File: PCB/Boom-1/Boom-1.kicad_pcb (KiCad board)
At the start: 2 copper layers, 698 parts, among them J1 NoiseIOConn, J10 Osc1HFTrackConn, J11 Osc1FiltCVConn, J12 OscFiltEnv1Conn, J13 OscFiltEnv2Conn, J14 SubFiltEnv1Conn, J15 SubFiltEnv2Conn, J16 Osc1FXConn, J17 SubFXConn, J18 Osc1FiltCVConn, J19 Osc1FiltCVConn, J2 Osc2CVConn, J20 Osc2FXConn, J21 OscAmpEnvConn, J22 SubAmpEnvConn, J23 OscAmpEnvBypass, J24 SubAmpAudioBypass, J25 SubAmpEnvBypass, J26 PreFV1FXConn, J27 PowerConn, J28 FV1Conn, J29 IOConn, J3 Osc1CVConn, J4 Osc2SyncConn, J5 Osc1SyncConn, J6 Osc2ScaleConn, J7 Osc2HFTrackConn, J8 SubIOConn, J9 Osc1ScaleConn, Q1 2N3904, SW1 SW_DIP_x04, U1 CEM3340, U10 AS3320, U11 AS3310, U12 AS3310, U13 AS3310, U14 AS3310, U15 V2164D, U16 AS3310, U17 AS3310, U18 V2164D, U19 TL074, U2 CEM3340, U20 TL074, U21 TL074, U22 TL074, U23 TL074, U24 TL074, U25 TL074, U26 TL074, U27 TL072, U28 TL074, U29 TL072, U3 4013, U30 TL074, U31 TL072, U32 TL074, U33 TL074, U34 TL074, U35 TL072, U36 TL074, U37 TL074, U38 TL072, U39 TL074, U4 NOISE, U40 TL072, U41 TL074, U42 TL074, U43 TL074, U44 TL074, U45 L7905, U46 L7805, U5 V2164D, U6 V2164D, U7 V2164D, U8 AS3320, U9 AS3320

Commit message: gathered componets for osc filt env 1
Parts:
- moved C86 1592.8 mm to (-516.1, -276.1)
- moved C55 1568.3 mm to (-506.5, -297.4)
- moved C61 1563.3 mm to (-515.9, -280.4)
- moved C85 1559.6 mm to (-496.1, -278.1)
- moved C69 1541.4 mm to (-483.9, -280.9)
- moved R173 1541.4 mm to (-486.2, -294.9)
- moved C57 1536.9 mm to (-516.1, -271.0)
- moved C70 1530.4 mm to (-465.8, -280.9)
- moved R182 1529.3 mm to (-487.4, -262.9)
- moved R176 1528.5 mm to (-486.2, -288.5)
- moved C78 1526.4 mm to (-442.7, -273.1), turned to 180 degrees
- moved R208 1518.1 mm to (-465.8, -273.1)
- moved C77 1512.7 mm to (-424.9, -280.7), turned to 180 degrees
- moved R148 1509.6 mm to (-511.0, -288.0), turned to 180 degrees
- moved R206 1508.2 mm to (-494.0, -285.5)
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
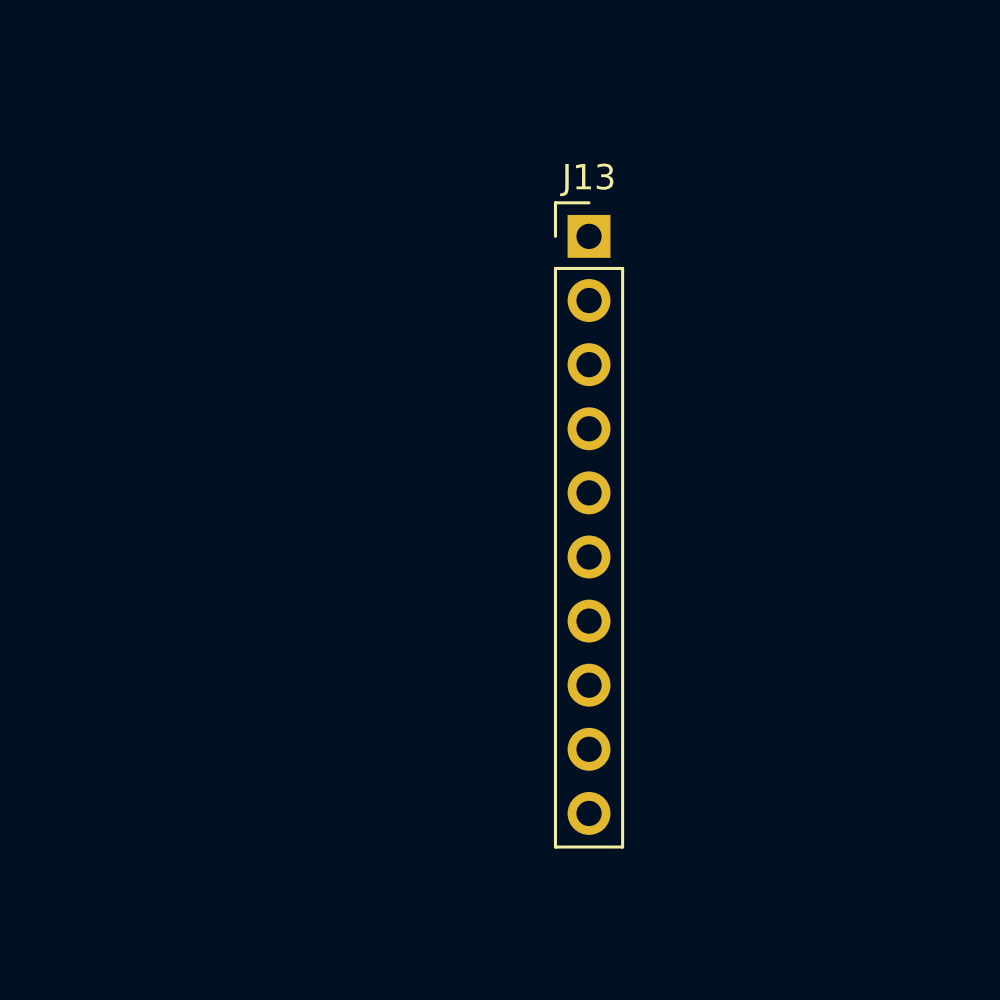
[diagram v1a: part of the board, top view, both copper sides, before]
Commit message: gathered componets for osc filt env 1
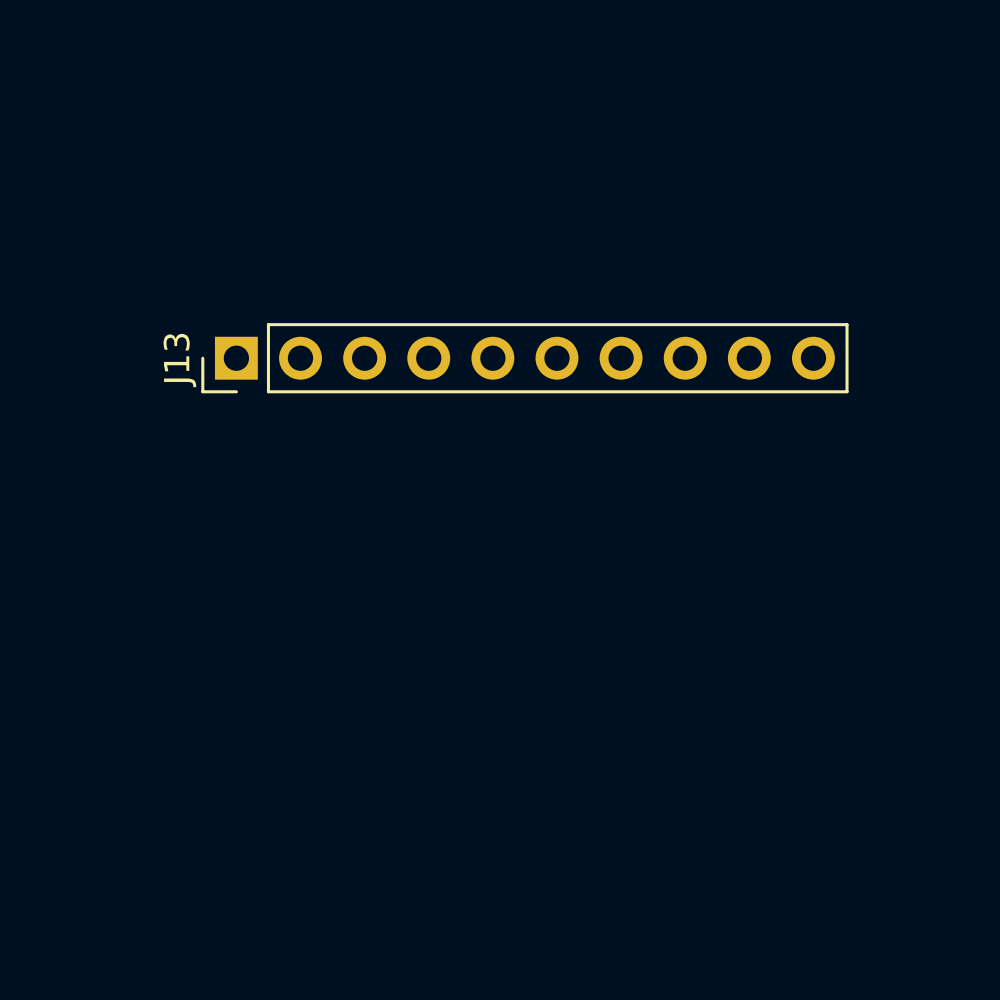
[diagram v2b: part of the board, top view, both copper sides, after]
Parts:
- moved J13 14.8 mm to (-478.3, -178.3), turned to 90 degrees
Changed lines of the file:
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@@
   )
   (module Connector_PinHeader_2.54mm:PinHeader_1x10_P2.54mm_Vertical (layer F.Cu)
-    (at -464.312 -183.134)
+    (at -478.282 -178.308 90)
     (descr "Through hole straight pin header, 1x10, 2.54mm pitch, single row")
     (tags "Through hole pin header THT 1x10 2.54mm single row")
-    (fp_text reference J13 (at 0 -2.33) (layer F.SilkS)
+    (fp_text reference J13 (at 0 -2.33 90) (layer F.SilkS)
       (effects (font (size 1 1) (thickness 0.15)))
     )
-    (fp_text value OscFiltEnv2Conn (at 0 25.19) (layer F.Fab)
+    (fp_text value OscFiltEnv2Conn (at 0 25.19 90) (layer F.Fab)
       (effects (font (size 1 1) (thickness 0.15)))
     )
@@
     (fp_line (start 1.8 24.65) (end 1.8 -1.8) (layer F.CrtYd) (width 0.05))
     (fp_line (start 1.8 -1.8) (end -1.8 -1.8) (layer F.CrtYd) (width 0.05))
-    (fp_text user %R (at 0 11.43 90) (layer F.Fab)
+    (fp_text user %R (at 0 11.43) (layer F.Fab)
       (effects (font (size 1 1) (thickness 0.15)))
     )
-    (pad 10 thru_hole oval (at 0 22.86) (size 1.7 1.7) (drill 1) (layers *.Cu *.Mask)
+    (pad 10 thru_hole oval (at 0 22.86 90) (size 1.7 1.7) (drill 1) (layers *.Cu *.Mask)
       (net 160 "Net-(J13-Pad10)"))
-    (pad 9 thru_hole oval (at 0 20.32) (size 1.7 1.7) (drill 1) (layers *.Cu *.Mask)
+    (pad 9 thru_hole oval (at 0 20.32 90) (size 1.7 1.7) (drill 1) (layers *.Cu *.Mask)
       (net 161 "Net-(J13-Pad9)"))
-    (pad 8 thru_hole oval (at 0 17.78) (size 1.7 1.7) (drill 1) (layers *.Cu *.Mask)
+    (pad 8 thru_hole oval (at 0 17.78 90) (size 1.7 1.7) (drill 1) (layers *.Cu *.Mask)
       (net 162 "Net-(J13-Pad8)"))
-    (pad 7 thru_hole oval (at 0 15.24) (size 1.7 1.7) (drill 1) (layers *.Cu *.Mask)
+    (pad 7 thru_hole oval (at 0 15.24 90) (size 1.7 1.7) (drill 1) (layers *.Cu *.Mask)
       (net 163 "Net-(J13-Pad7)"))
-    (pad 6 thru_hole oval (at 0 12.7) (size 1.7 1.7) (drill 1) (layers *.Cu *.Mask)
+    (pad 6 thru_hole oval (at 0 12.7 90) (size 1.7 1.7) (drill 1) (layers *.Cu *.Mask)
       (net 164 "Net-(J13-Pad6)"))
-    (pad 5 thru_hole oval (at 0 10.16) (size 1.7 1.7) (drill 1) (layers *.Cu *.Mask)
+    (pad 5 thru_hole oval (at 0 10.16 90) (size 1.7 1.7) (drill 1) (layers *.Cu *.Mask)
       (net 165 "Net-(J13-Pad5)"))
-    (pad 4 thru_hole oval (at 0 7.62) (size 1.7 1.7) (drill 1) (layers *.Cu *.Mask)
+    (pad 4 thru_hole oval (at 0 7.62 90) (size 1.7 1.7) (drill 1) (layers *.Cu *.Mask)
       (net 166 "Net-(J13-Pad4)"))
-    (pad 3 thru_hole oval (at 0 5.08) (size 1.7 1.7) (drill 1) (layers *.Cu *.Mask)
+    (pad 3 thru_hole oval (at 0 5.08 90) (size 1.7 1.7) (drill 1) (layers *.Cu *.Mask)
       (net 167 "Net-(J13-Pad3)"))
-    (pad 2 thru_hole oval (at 0 2.54) (size 1.7 1.7) (drill 1) (layers *.Cu *.Mask)
+    (pad 2 thru_hole oval (at 0 2.54 90) (size 1.7 1.7) (drill 1) (layers *.Cu *.Mask)
       (net 168 "Net-(J13-Pad2)"))
-    (pad 1 thru_hole rect (at 0 0) (size 1.7 1.7) (drill 1) (layers *.Cu *.Mask)
+    (pad 1 thru_hole rect (at 0 0 90) (size 1.7 1.7) (drill 1) (layers *.Cu *.Mask)
       (net 1 GND))
     (model ${KISYS3DMOD}/Connector_PinHeader_2.54mm.3dshapes/PinHeader_1x10_P2.54mm_Vertical.wrl

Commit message: gathered componets for osc filt env 2
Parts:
- moved C82 1555.2 mm to (-500.1, -232.2), turned to 180 degrees
- moved C56 1542.6 mm to (-515.4, -225.6)
- moved C81 1533.6 mm to (-505.7, -201.4)
- moved C58 1528.0 mm to (-515.6, -207.8)
- moved C62 1503.3 mm to (-515.1, -215.4)
- moved C68 1496.9 mm to (-474.5, -196.3)
- moved R152 1492.3 mm to (-496.3, -210.3)
- moved R207 1484.4 mm to (-467.4, -230.9), turned to 180 degrees
- moved R195 1484.0 mm to (-458.2, -224.5), turned to 180 degrees
- moved R174 1477.2 mm to (-486.9, -230.9)
- moved R185 1476.9 mm to (-458.2, -227.8)
- moved R228 1476.4 mm to (-455.4, -210.3)
- moved R149 1473.9 mm to (-516.4, -218.2), turned to 180 degrees
- moved C67 1471.1 mm to (-474.5, -202.7)
- moved R231 1469.9 mm to (-461.3, -216.9)
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
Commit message: gathered parts for sub filt env 1 and 2
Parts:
- moved C65 1323.3 mm to (-492.3, 236.7)
- moved C74 1299.9 mm to (-507.0, 350.3)
- moved R159 1287.0 mm to (-503.2, 249.2), turned to 180 degrees
- moved C66 1284.3 mm to (-501.9, 339.9), turned to 180 degrees
- moved C72 1274.6 mm to (-507.0, 357.6)
- moved R233 1268.0 mm to (-460.5, 242.3)
- moved C71 1261.3 mm to (-500.4, 259.3)
- moved R196 1260.0 mm to (-460.5, 238.0)
- moved R211 1242.9 mm to (-430.3, 238.0)
- moved C73 1236.4 mm to (-495.3, 251.7), turned to 180 degrees
- moved R199 1219.5 mm to (-463.0, 355.9)
- moved R210 1218.8 mm to (-430.0, 253.2)
- moved R212 1212.8 mm to (-430.3, 358.4)
- moved R221 1210.8 mm to (-432.6, 238.0), turned to 180 degrees
- moved R165 1206.7 mm to (-488.7, 355.1)
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
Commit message: gathered parts for osc amp env
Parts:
- moved C118 1109.2 mm to (-55.6, -82.8), turned to 180 degrees
- moved C120 1097.3 mm to (-60.7, -65.0)
- moved C115 1093.5 mm to (-60.7, -69.1)
- moved C122 1091.2 mm to (-55.6, -72.1), turned to 180 degrees
- moved C114 1089.1 mm to (-37.3, -70.6), turned to 180 degrees
- moved C143 1059.8 mm to (-8.64, -70.1), turned to 180 degrees
- moved C142 1055.9 mm to (8.64, -77.7), turned to 180 degrees
- moved C126 1028.1 mm to (45.0, -69.3)
- moved R267 1019.5 mm to (-55.6, -75.2), turned to 180 degrees
- moved C127 1014.3 mm to (62.5, -69.3)
- moved R269 998.6 mm to (-42.4, -67.6)
- moved R302 978.1 mm to (32.5, -65.0)
- moved R289 974.9 mm to (40.1, -62.0), turned to 180 degrees
- moved R308 962.8 mm to (42.4, -65.0)
- moved R290 958.9 mm to (79.5, -74.2), turned to 180 degrees
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
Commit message: power units for amp and filt envs
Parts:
- moved C88 1263.5 mm to (-452.9, 245.6), turned to 180 degrees
- moved C89 1224.0 mm to (-440.4, 245.6)
- moved C100 1180.6 mm to (-457.2, 296.4)
- moved C132 991.5 mm to (7.11, 20.6)
- moved C130 979.2 mm to (-11.9, 32.3)
- moved C133 964.5 mm to (24.6, 20.6)
- moved C135 961.8 mm to (5.59, 66.3)
- moved C137 955.7 mm to (-9.65, 53.8), turned to 180 degrees
- moved C134 950.8 mm to (27.9, 58.7), turned to 180 degrees
- moved C116 937.5 mm to (-17.5, 144.5)
- moved C117 923.9 mm to (-30.7, 144.5), turned to 180 degrees
- moved R277 919.7 mm to (-22.4, 25.4)
- moved C124 913.9 mm to (11.9, 140.5)
- moved C125 899.6 mm to (29.2, 140.5)
- moved C140 896.8 mm to (8.64, 173.7)
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
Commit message: gathered parts for osc amp
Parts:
- moved TP34 1046.6 mm to (-44.7, 31.0)
- moved C139 999.5 mm to (11.9, 25.9), turned to 270 degrees
- moved C128 996.6 mm to (-33.0, 30.5), turned to 180 degrees
- moved TP37 991.4 mm to (14.7, 35.6)
- moved C129 987.5 mm to (-31.8, 62.0), turned to 90 degrees
- moved R279 941.4 mm to (-37.3, 24.4)
- moved R278 917.4 mm to (-32.8, 39.9)
- moved R271 910.5 mm to (-25.1, 34.8), turned to 180 degrees
- moved R287 909.8 mm to (-35.6, 37.1), turned to 180 degrees
- moved R301 908.2 mm to (7.11, 25.7), turned to 270 degrees
- moved R272 905.2 mm to (-32.8, 47.5)
- moved R274 904.1 mm to (-25.1, 55.6), turned to 270 degrees
- moved R310 897.1 mm to (12.4, 13.0), turned to 180 degrees
- moved R315 881.2 mm to (29.7, 34.0)
- moved R316 873.4 mm to (24.6, 28.7)
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
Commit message: gathered parts for sub amp
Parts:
- moved C131 1001.2 mm to (-5.08, 17.8), turned to 180 degrees
- moved TP35 994.7 mm to (-3.30, 58.9)
- moved TP36 992.5 mm to (-7.62, 65.8)
- moved C145 985.5 mm to (10.2, 50.0)
- moved TP38 984.6 mm to (19.1, 51.1)
- moved C144 961.7 mm to (32.3, 61.5), turned to 270 degrees
- moved C136 952.3 mm to (7.37, 48.0), turned to 180 degrees
- moved R275 923.3 mm to (-11.2, 24.6)
- moved R273 910.4 mm to (-11.7, 47.2)
- moved R284 902.4 mm to (-0.25, 42.9)
- moved R291 901.8 mm to (-4.57, 29.7)
- moved R286 901.7 mm to (-4.32, 39.9), turned to 180 degrees
- moved R299 891.0 mm to (-3.30, 36.3)
- moved R307 888.9 mm to (5.33, 54.9)
- moved R313 857.4 mm to (32.3, 55.9)
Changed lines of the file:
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@@
   )
   (module Capacitor_THT:C_Disc_D5.0mm_W2.5mm_P5.00mm (layer F.Cu)
-    (at 719.203451 708.954495)
+    (at -5.08 17.78 180)
     (descr "C, Disc series, Radial, pin pitch=5.00mm, , diameter*width=5*2.5mm^2, Capacitor, http://cdn-reichelt.de/documents/datenblatt/B300/DS_KERKO_TC.pdf")
     (tags "C Disc series Radial pin pitch 5.00mm  diameter 5mm width 2.5mm Capacitor")
@@
       (effects (font (size 1 1) (thickness 0.15)))
     )
-    (pad 1 thru_hole circle (at 0 0) (size 1.6 1.6) (drill 0.8) (layers *.Cu *.Mask)
+    (pad 1 thru_hole circle (at 0 0 180) (size 1.6 1.6) (drill 0.8) (layers *.Cu *.Mask)
       (net 87 "Net-(C131-Pad1)"))
-    (pad 2 thru_hole circle (at 5 0) (size 1.6 1.6) (drill 0.8) (layers *.Cu *.Mask)
+    (pad 2 thru_hole circle (at 5 0 180) (size 1.6 1.6) (drill 0.8) (layers *.Cu *.Mask)
       (net 1 GND))
     (model ${KISYS3DMOD}/Capacitor_THT.3dshapes/C_Disc_D5.0mm_W2.5mm_P5.00mm.wrl
@@
   )
   (module Capacitor_THT:C_Disc_D5.0mm_W2.5mm_P5.00mm (layer F.Cu)
-    (at 606.065301 788.560569)
+    (at 7.366 48.006 180)
     (descr "C, Disc series, Radial, pin pitch=5.00mm, , diameter*width=5*2.5mm^2, Capacitor, http://cdn-reichelt.de/documents/datenblatt/B300/DS_KERKO_TC.pdf")
     (tags "C Disc series Radial pin pitch 5.00mm  diameter 5mm width 2.5mm Capacitor")
@@
       (effects (font (size 1 1) (thickness 0.15)))
     )
-    (pad 2 thru_hole circle (at 5 0) (size 1.6 1.6) (drill 0.8) (layers *.Cu *.Mask)
+    (pad 2 thru_hole circle (at 5 0 180) (size 1.6 1.6) (drill 0.8) (layers *.Cu *.Mask)
       (net 1 GND))
-    (pad 1 thru_hole circle (at 0 0) (size 1.6 1.6) (drill 0.8) (layers *.Cu *.Mask)
+    (pad 1 thru_hole circle (at 0 0 180) (size 1.6 1.6) (drill 0.8) (layers *.Cu *.Mask)
       (net 88 "Net-(C136-Pad1)"))
     (model ${KISYS3DMOD}/Capacitor_THT.3dshapes/C_Disc_D5.0mm_W2.5mm_P5.00mm.wrl
@@
   )
   (module Capacitor_THT:C_Disc_D5.0mm_W2.5mm_P2.50mm (layer F.Cu)
-    (at 711.816951 741.937697)
+    (at 32.258 61.468 270)
     (descr "C, Disc series, Radial, pin pitch=2.50mm, , diameter*width=5*2.5mm^2, Capacitor, http://cdn-reichelt.de/documents/datenblatt/B300/DS_KERKO_TC.pdf")
     (tags "C Disc series Radial pin pitch 2.50mm  diameter 5mm width 2.5mm Capacitor")
-    (fp_text reference C144 (at 1.25 -2.5) (layer F.SilkS)
+    (fp_text reference C144 (at 1.25 -2.5 90) (layer F.SilkS)
       (effects (font (size 1 1) (thickness 0.15)))
     )
-    (fp_text value 100pF (at 1.25 2.5) (layer F.Fab)
+    (fp_text value 100pF (at 1.25 2.5 90) (layer F.Fab)
       (effects (font (size 1 1) (thickness 0.15)))
     )
@@
     (fp_line (start 4 1.5) (end 4 -1.5) (layer F.CrtYd) (width 0.05))
     (fp_line (start 4 -1.5) (end -1.5 -1.5) (layer F.CrtYd) (width 0.05))
-    (fp_text user %R (at 1.25 0) (layer F.Fab)
+    (fp_text user %R (at 1.25 0 90) (layer F.Fab)
       (effects (font (size 1 1) (thickness 0.15)))
     )
-    (pad 1 thru_hole circle (at 0 0) (size 1.6 1.6) (drill 0.8) (layers *.Cu *.Mask)
+    (pad 1 thru_hole circle (at 0 0 270) (size 1.6 1.6) (drill 0.8) (layers *.Cu *.Mask)
       (net 93 "Net-(C144-Pad1)"))
-    (pad 2 thru_hole circle (at 2.5 0) (size 1.6 1.6) (drill 0.8) (layers *.Cu *.Mask)
+    (pad 2 thru_hole circle (at 2.5 0 270) (size 1.6 1.6) (drill 0.8) (layers *.Cu *.Mask)
       (net 94 "Net-(C144-Pad2)"))
     (model ${KISYS3DMOD}/Capacitor_THT.3dshapes/C_Disc_D5.0mm_W2.5mm_P2.50mm.wrl
@@
   )
   (module Capacitor_THT:C_Disc_D5.0mm_W2.5mm_P2.50mm (layer F.Cu)
-    (at 765.795076 682.667131)
+    (at 10.16 50.038)
     (descr "C, Disc series, Radial, pin pitch=2.50mm, , diameter*width=5*2.5mm^2, Capacitor, http://cdn-reichelt.de/documents/datenblatt/B300/DS_KERKO_TC.pdf")
     (tags "C Disc series Radial pin pitch 2.50mm  diameter 5mm width 2.5mm Capacitor")
@@
   )
   (module Resistor_THT:R_Axial_DIN0207_L6.3mm_D2.5mm_P7.62mm_Horizontal (layer F.Cu)
-    (at 522.708551 784.344671)
+    (at -11.684 47.244)
     (descr "Resistor, Axial_DIN0207 series, Axial, Horizontal, pin pitch=7.62mm, 0.25W = 1/4W, length*diameter=6.3*2.5mm^2, http://cdn-reichelt.de/documents/datenblatt/B400/1_4W%23YAG.pdf")
     (tags "Resistor Axial_DIN0207 series Axial Horizontal pin pitch 7.62mm 0.25W = 1/4W length 6.3mm diameter 2.5mm")
@@
   )
   (module Resistor_THT:R_Axial_DIN0207_L6.3mm_D2.5mm_P7.62mm_Horizontal (layer F.Cu)
-    (at 530.049576 772.688953)
+    (at -11.176 24.638)
     (descr "Resistor, Axial_DIN0207 series, Axial, Horizontal, pin pitch=7.62mm, 0.25W = 1/4W, length*diameter=6.3*2.5mm^2, http://cdn-reichelt.de/documents/datenblatt/B400/1_4W%23YAG.pdf")
     (tags "Resistor Axial_DIN0207 series Axial Horizontal pin pitch 7.62mm 0.25W = 1/4W length 6.3mm diameter 2.5mm")
@@
   )
   (module Resistor_THT:R_Axial_DIN0207_L6.3mm_D2.5mm_P7.62mm_Horizontal (layer F.Cu)
-    (at 675.393001 641.083001)
+    (at -0.254 42.926)
     (descr "Resistor, Axial_DIN0207 series, Axial, Horizontal, pin pitch=7.62mm, 0.25W = 1/4W, length*diameter=6.3*2.5mm^2, http://cdn-reichelt.de/documents/datenblatt/B400/1_4W%23YAG.pdf")
     (tags "Resistor Axial_DIN0207 series Axial Horizontal pin pitch 7.62mm 0.25W = 1/4W length 6.3mm diameter 2.5mm")
@@
   )
   (module Resistor_THT:R_Axial_DIN0207_L6.3mm_D2.5mm_P7.62mm_Horizontal (layer F.Cu)
-    (at 659.165251 650.427911)
+    (at -4.318 39.878 180)
     (descr "Resistor, Axial_DIN0207 series, Axial, Horizontal, pin pitch=7.62mm, 0.25W = 1/4W, length*diameter=6.3*2.5mm^2, http://cdn-reichelt.de/documents/datenblatt/B400/1_4W%23YAG.pdf")
     (tags "Resistor Axial_DIN0207 series Axial Horizontal pin pitch 7.62mm 0.25W = 1/4W length 6.3mm diameter 2.5mm")
@@
       (effects (font (size 1 1) (thickness 0.15)))
     )
-    (pad 2 thru_hole oval (at 7.62 0) (size 1.6 1.6) (drill 0.8) (layers *.Cu *.Mask)
+    (pad 2 thru_hole oval (at 7.62 0 180) (size 1.6 1.6) (drill 0.8) (layers *.Cu *.Mask)
       (net 94 "Net-(C144-Pad2)"))
-    (pad 1 thru_hole circle (at 0 0) (size 1.6 1.6) (drill 0.8) (layers *.Cu *.Mask)
+    (pad 1 thru_hole circle (at 0 0 180) (size 1.6 1.6) (drill 0.8) (layers *.Cu *.Mask)
       (net 214 /CVInput))
     (model ${KISYS3DMOD}/Resistor_THT.3dshapes/R_Axial_DIN0207_L6.3mm_D2.5mm_P7.62mm_Horizontal.wrl
@@
   )
   (module Resistor_THT:R_Axial_DIN0207_L6.3mm_D2.5mm_P7.62mm_Horizontal (layer F.Cu)
-    (at 640.596776 659.851683)
+    (at -4.572 29.718)
     (descr "Resistor, Axial_DIN0207 series, Axial, Horizontal, pin pitch=7.62mm, 0.25W = 1/4W, length*diameter=6.3*2.5mm^2, http://cdn-reichelt.de/documents/datenblatt/B400/1_4W%23YAG.pdf")
     (tags "Resistor Axial_DIN0207 series Axial Horizontal pin pitch 7.62mm 0.25W = 1/4W length 6.3mm diameter 2.5mm")
@@
   )
   (module Resistor_THT:R_Axial_DIN0207_L6.3mm_D2.5mm_P7.62mm_Horizontal (layer F.Cu)
-    (at 546.458926 737.473805)
+    (at -3.302 36.322)
     (descr "Resistor, Axial_DIN0207 series, Axial, Horizontal, pin pitch=7.62mm, 0.25W = 1/4W, length*diameter=6.3*2.5mm^2, http://cdn-reichelt.de/documents/datenblatt/B400/1_4W%23YAG.pdf")
     (tags "Resistor Axial_DIN0207 series Axial Horizontal pin pitch 7.62mm 0.25W = 1/4W length 6.3mm diameter 2.5mm")
@@
   )
   (module Resistor_THT:R_Axial_DIN0207_L6.3mm_D2.5mm_P7.62mm_Horizontal (layer F.Cu)
-    (at 519.685776 779.880779)
+    (at 5.334 54.864)
     (descr "Resistor, Axial_DIN0207 series, Axial, Horizontal, pin pitch=7.62mm, 0.25W = 1/4W, length*diameter=6.3*2.5mm^2, http://cdn-reichelt.de/documents/datenblatt/B400/1_4W%23YAG.pdf")
     (tags "Resistor Axial_DIN0207 series Axial Horizontal pin pitch 7.62mm 0.25W = 1/4W length 6.3mm diameter 2.5mm")
@@
   )
   (module Resistor_THT:R_Axial_DIN0207_L6.3mm_D2.5mm_P7.62mm_Horizontal (layer F.Cu)
-    (at 532.640526 752.105451)
+    (at 32.258 55.88)
     (descr "Resistor, Axial_DIN0207 series, Axial, Horizontal, pin pitch=7.62mm, 0.25W = 1/4W, length*diameter=6.3*2.5mm^2, http://cdn-reichelt.de/documents/datenblatt/B400/1_4W%23YAG.pdf")
     (tags "Resistor Axial_DIN0207 series Axial Horizontal pin pitch 7.62mm 0.25W = 1/4W length 6.3mm diameter 2.5mm")
@@
   )
   (module Connector_PinHeader_2.54mm:PinHeader_1x01_P2.54mm_Vertical (layer F.Cu)
-    (at 716.089726 745.905601)
+    (at -3.302 58.928)
     (descr "Through hole straight pin header, 1x01, 2.54mm pitch, single row")
     (tags "Through hole pin header THT 1x01 2.54mm single row")
@@
   )
   (module Connector_PinHeader_2.54mm:PinHeader_1x01_P2.54mm_Vertical (layer F.Cu)
-    (at 709.612351 751.857457)
+    (at -7.62 65.786)
     (descr "Through hole straight pin header, 1x01, 2.54mm pitch, single row")
     (tags "Through hole pin header THT 1x01 2.54mm single row")
@@
   )
   (module Connector_PinHeader_2.54mm:PinHeader_1x01_P2.54mm_Vertical (layer F.Cu)
-    (at 759.272226 700.274705)
+    (at 19.05 51.054)
     (descr "Through hole straight pin header, 1x01, 2.54mm pitch, single row")
     (tags "Through hole pin header THT 1x01 2.54mm single row")
